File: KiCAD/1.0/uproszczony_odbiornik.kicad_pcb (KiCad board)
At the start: 2 copper layers, 47 x 52 mm, 57 parts, among them IC4 DSPIC33FJ64MC804-PT, Q1 10MHz, Y1 CMR309T

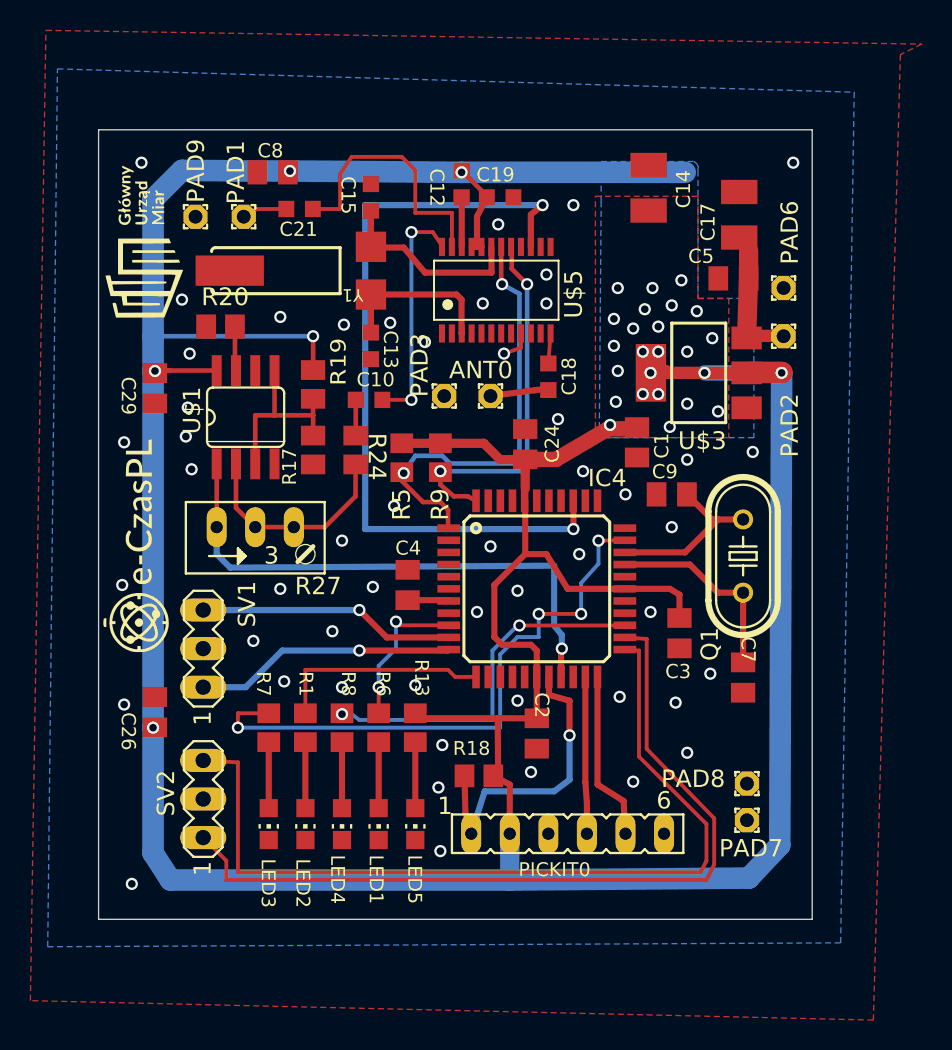
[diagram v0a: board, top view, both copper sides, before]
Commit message: fix schematics and PCB, Add R2
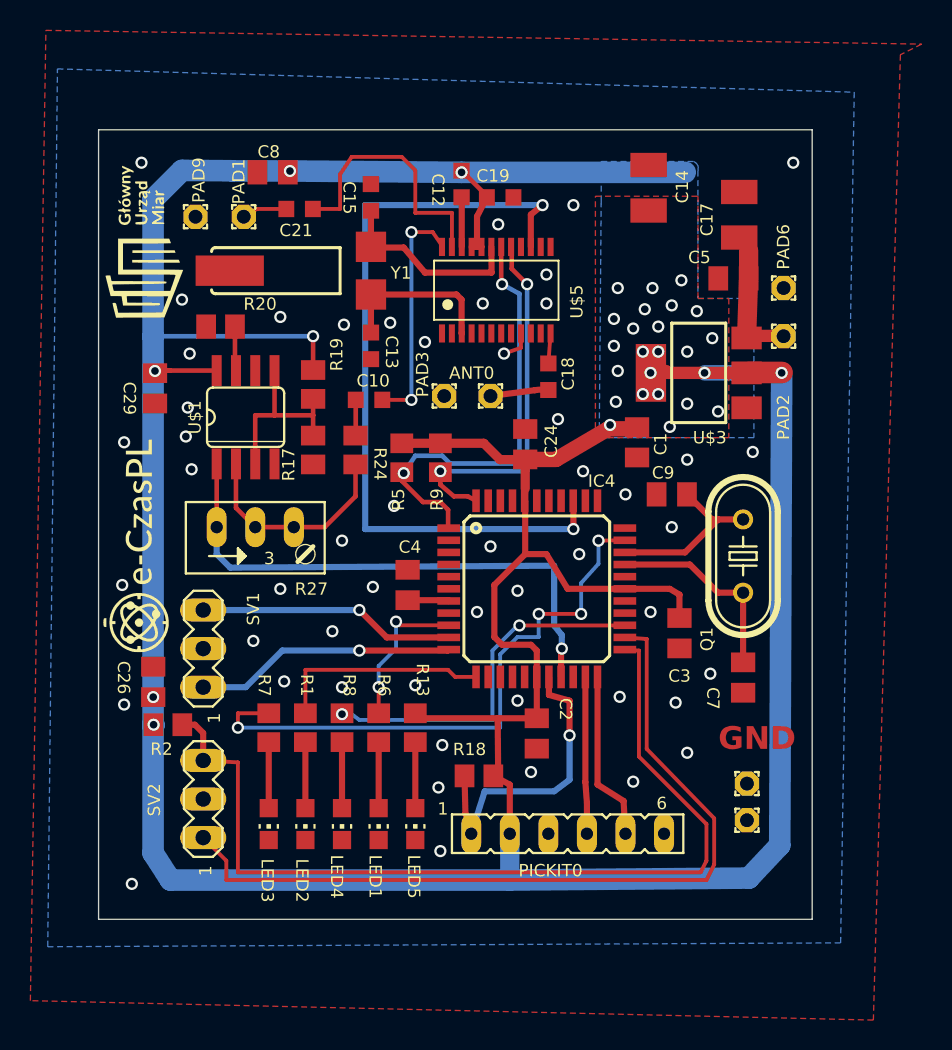
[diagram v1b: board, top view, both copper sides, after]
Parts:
- added R2: 20k, uproszczony_odbiornik:R0805, F.Cu at (129.6, 118.2)
- moved C26 2.00 mm to (128.6, 115.4)
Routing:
- net Net-(IC4-AN4/C1IN-/RP2/CN6/RB2): track 57.5 -> 61.0 mm
- net VDD: track 264.4 -> 263.9 mm, vias 30 -> 31
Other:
- board text added: "GND"

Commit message: change read.me
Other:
- board text added: "+5V"
- board text added: "NMEA"
- board text added: "T1kHz"
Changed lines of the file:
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@@
 		(descr "Hyper CHIPLED Hyper-Bright LED\n\nLB R99A\nSource: http://www.osram.convergy.de/ ... lb_r99a.pdf")
 		(property "Reference" "LED2"
-			(at 0.7001 -2.2674 -90)
+			(at 0.7001 -2.0134 -90)
 			(unlocked yes)
 			(layer "F.SilkS")
@@
 			(unlocked yes)
 			(layer "F.SilkS")
+			(hide yes)
 			(effects
 				(font
@@
 		(descr "Hyper CHIPLED Hyper-Bright LED\n\nLB R99A\nSource: http://www.osram.convergy.de/ ... lb_r99a.pdf")
 		(property "Reference" "LED3"
-			(at 0.5731 -2.2674 -90)
+			(at 0.5731 -2.0134 -90)
 			(unlocked yes)
 			(layer "F.SilkS")
@@
 		(descr "THROUGH-HOLE PAD")
 		(property "Reference" "ANT0"
-			(at -2.7321 -1.0346 0)
+			(at -1.3351 -1.1616 0)
 			(unlocked yes)
 			(layer "F.SilkS")
@@
 		(descr "Ceramic Chip Capacitor KEMET 0805 reflow solder\n\nMetric Code Size 2012")
 		(property "Reference" "C5"
-			(at 2.9861 0.9076 0)
+			(at 3.1131 1.2378 0)
 			(unlocked yes)
 			(layer "F.SilkS")
@@
 			(unlocked yes)
 			(layer "F.SilkS")
+			(hide yes)
 			(effects
 				(font
@@
 			(unlocked yes)
 			(layer "F.SilkS")
+			(hide yes)
 			(effects
 				(font
@@
 			(unlocked yes)
 			(layer "F.SilkS")
+			(hide yes)
 			(effects
 				(font
@@
 			(unlocked yes)
 			(layer "F.SilkS")
+			(hide yes)
 			(effects
 				(font
@@
 		(layer "Edge.Cuts")
 	)
+	(gr_text "NMEA"
+		(at 126.7714 126.2126 0)
+		(layer "F.SilkS")
+		(effects
+			(font
+				(size 0.8128 0.8128)
+				(thickness 0.1524)
+				(bold yes)
+			)
+			(justify left bottom)
+		)
+	)
 	(gr_text "GND"
-		(at 165.8112 119.9642 0)
-		(layer "F.Cu")
+		(at 165.354 120.3706 0)
+		(layer "F.SilkS")
 		(effects
 			(font
@@
 				(bold yes)
 			)
+			(justify left bottom)
+		)
+	)
+	(gr_text "T1kHz"
+		(at 134.1882 83.566 90)
+		(layer "F.SilkS")
+		(effects
+			(font
+				(size 0.8128 0.8128)
+				(thickness 0.1524)
+				(bold yes)
+			)
+			(justify left bottom)
+		)
+	)
+	(gr_text "GND"
+		(at 170.5356 87.884 90)
+		(layer "F.SilkS")
+		(effects
+			(font
+				(size 0.8128 0.8128)
+				(thickness 0.1524)
+				(bold yes)
+			)
+			(justify left bottom)
+		)
+	)
+	(gr_text "+5V"
+		(at 170.6372 98.552 90)
+		(layer "F.SilkS")
+		(effects
+			(font
+				(size 0.8128 0.8128)
+				(thickness 0.1524)
+				(bold yes)
+			)
